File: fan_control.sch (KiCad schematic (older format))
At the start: 15 parts, among them M1 Fan, Q14 BC547, Q15 BC547, Q16 BC547, Q17 BC547, Q18 BC547

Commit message: footprint assoziation; pcb layout; and more
* delete mainboard pcb
* rearrange project files/names
* create pcb layout
* improve schematics
* more
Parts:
- removed Q14, Q15, Q16, Q17, Q18: BC547, Package_TO_SOT_THT:TO-92_Inline, symbol 0_project:BC547B
- removed R11, R15, R17, R19, R21: 10K, Resistor_THT:R_Axial_DIN0207_L6.3mm_D2.5mm_P15.24mm_Horizontal, symbol Device:R
- removed R14, R16, R18, R20: 22, Resistor_THT:R_Axial_DIN0207_L6.3mm_D2.5mm_P15.24mm_Horizontal, symbol Device:R
- added C2: elko, Capacitor_THT:CP_Radial_D5.0mm_P2.50mm, symbol 0_project:elko
- added D4: 1N4007, symbol Diode:1N4007
- added D6, D7, D8: 1N4007, Diode_THT:D_DO-41_SOD81_P2.54mm_Vertical_AnodeUp, symbol Diode:1N4007
- added Q2: IRFZ34N, Package_TO_SOT_THT:TO-220-3_Vertical, symbol 0_project:IRFZ34N
- added R2, R3: R, Resistor_THT:R_Axial_DIN0207_L6.3mm_D2.5mm_P2.54mm_Vertical, symbol Device:R
- added R4: 50k, Resistor_THT:R_Axial_DIN0207_L6.3mm_D2.5mm_P2.54mm_Vertical, symbol Device:R
- added U1: LM317_3PinPackage, Package_TO_SOT_THT:TO-220-3_Vertical, symbol Regulator_Linear:LM317_3PinPackage
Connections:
- net +15V: now also M1.1 (+), R2.2, U1.2 (VO)
- net multiplier/F+: now also Q2.2 (G), R4.1
- net GND: no longer names the net of M1.2 (-)
- net GND: now also Q2.1 (D)
- new net: C2.1, D7.1 (K), D8.1 (K), U1.3 (VI)
- new net: R2.1, R3.1, U1.1 (ADJ)
- new net +15VAC: D4.1 (K), D7.2 (A)
- new net 0: C2.2, D4.2 (A), D6.2 (A), Q2.3 (S), R3.2, R4.2
- new net 0VAC: D6.1 (K), D8.2 (A)
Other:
- note added: "Fan Transistor"
- moved on the sheet: M1

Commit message: progress on schematics
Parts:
- removed M1: Fan, Connector_PinHeader_2.54mm:PinHeader_1x02_P2.54mm_Vertical, symbol Motor:Fan
- removed Q2: IRFZ34N, Package_TO_SOT_THT:TO-220-3_Vertical, symbol 0_project:IRFZ34N
- removed R4: 50k, Resistor_THT:R_Axial_DIN0207_L6.3mm_D2.5mm_P2.54mm_Vertical, symbol Device:R
- added J1, J2, J3, J4, J5, J6, J7, J8: Conn_01x02_Male, Connector_PinHeader_2.54mm:PinHeader_1x02_P2.54mm_Vertical, symbol Connector:Conn_01x02_Male
- D4: footprint (none) -> Diode_THT:D_DO-41_SOD81_P2.54mm_Vertical_AnodeUp
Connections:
- net +15V: now also J4.1 (Pin_1), J4.2 (Pin_2)
- net +15VAC: now also J6.1 (Pin_1), J6.2 (Pin_2)
- net 0: now also J5.1 (Pin_1), J5.2 (Pin_2)
- net 0VAC: now also J8.1 (Pin_1), J8.2 (Pin_2)
- net B: now also J2.1 (Pin_1), J2.2 (Pin_2)
- net C: now also J3.1 (Pin_1), J3.2 (Pin_2)
- net E: now also J1.1 (Pin_1), J1.2 (Pin_2)
- new net F+: J7.1 (Pin_1), J7.2 (Pin_2)
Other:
- note removed: "Fan Transistor"
- moved on the sheet: R2, R3, U1

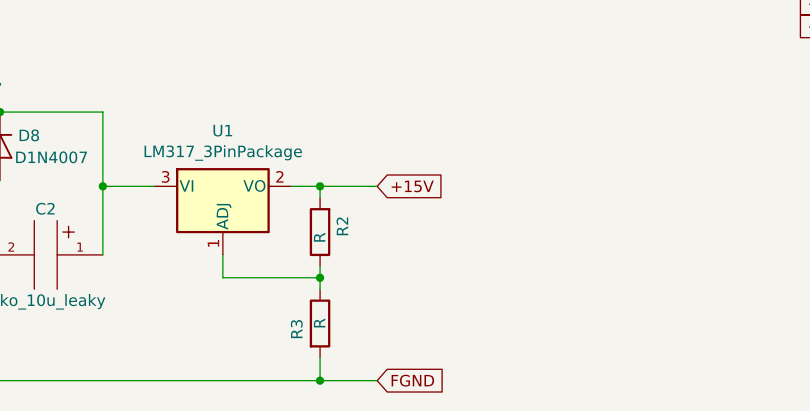
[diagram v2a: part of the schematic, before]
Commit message: add adjustment resistors
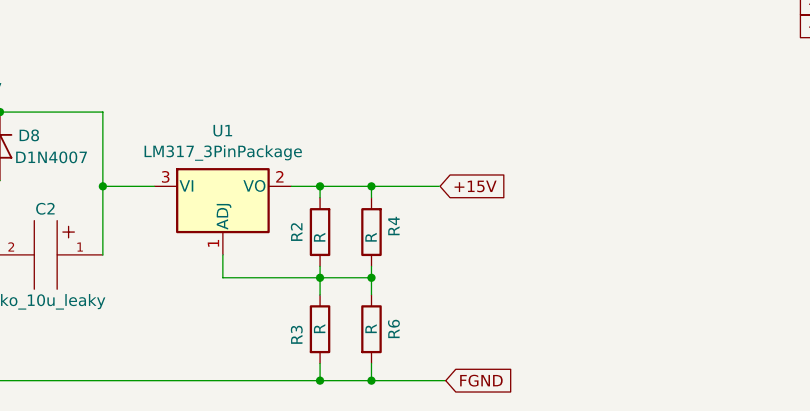
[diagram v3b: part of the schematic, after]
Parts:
- added R4, R6: R, Resistor_THT:R_Axial_DIN0207_L6.3mm_D2.5mm_P2.54mm_Vertical, symbol Device:R
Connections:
- net +15V: now also R4.2
- net 0: now also R6.2
- net at R2.1, R3.1, U1.1 (ADJ): now also R4.1, R6.1
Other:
- moved on the sheet: R3
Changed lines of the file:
@@
 L Device:R R3
 U 1 1 5EB4ABA5
-P 3250 4625
-F 0 "R3" V 3150 4600 50  0000 C CNN
-F 1 "R" V 3250 4625 50  0000 C CNN
-F 2 "Resistor_THT:R_Axial_DIN0207_L6.3mm_D2.5mm_P2.54mm_Vertical" V 3180 4625 50  0001 C CNN
-F 3 "~" H 3250 4625 50  0001 C CNN
-F 4 "N" H 3250 4625 50  0001 C CNN "Spice_Netlist_Enabled"
-	1    3250 4625
+P 3250 4650
+F 0 "R3" V 3150 4625 50  0000 C CNN
+F 1 "R" V 3250 4650 50  0000 C CNN
+F 2 "Resistor_THT:R_Axial_DIN0207_L6.3mm_D2.5mm_P2.54mm_Vertical" V 3180 4650 50  0001 C CNN
+F 3 "~" H 3250 4650 50  0001 C CNN
+F 4 "N" H 3250 4650 50  0001 C CNN "Spice_Netlist_Enabled"
+	1    3250 4650
 	1    0    0    -1
 $EndComp
@@
 	2825 4425 2825 4325
 Wire Wire Line
-	3250 4775 3250 4875
+	3250 4800 3250 4875
 Connection ~ 3250 4425
 Wire Wire Line
-	3250 4425 3250 4475
+	3250 4425 3250 4500
 Wire Wire Line
 	3250 4025 3250 4075
@@
 U 1 1 5EB4ABB4
 P 3250 4225
-F 0 "R2" V 3150 4200 50  0000 C CNN
+F 0 "R2" V 3350 4225 50  0000 C CNN
 F 1 "R" V 3250 4250 50  0000 C CNN
 F 2 "Resistor_THT:R_Axial_DIN0207_L6.3mm_D2.5mm_P2.54mm_Vertical" V 3180 4225 50  0001 C CNN
@@
 Connection ~ 3250 4025
 Wire Wire Line
-	3250 4875 3500 4875
-Wire Wire Line
-	3250 4025 3500 4025
+	3250 4875 3475 4875
+Wire Wire Line
+	3250 4025 3475 4025
 Wire Wire Line
 	1400 4875 3250 4875
 Connection ~ 3250 4875
-Text GLabel 3500 4025 2    50   Input ~ 0
+Text GLabel 3775 4025 2    50   Input ~ 0
 +15V
-Text GLabel 3500 4875 2    50   Input ~ 0
+Text GLabel 3800 4875 2    50   Input ~ 0
 FGND
 Text HLabel 1350 3700 1    50   Input ~ 0
@@
 Text GLabel 1800 1525 2    50   Input ~ 0
 F+
+Wire Wire Line
+	3250 4425 3475 4425
+$Comp
+L Device:R R4
+U 1 1 5EC4696D
+P 3475 4225
+F 0 "R4" V 3375 4200 50  0000 C CNN
+F 1 "R" V 3475 4250 50  0000 C CNN
+F 2 "Resistor_THT:R_Axial_DIN0207_L6.3mm_D2.5mm_P2.54mm_Vertical" V 3405 4225 50  0001 C CNN
+F 3 "~" H 3475 4225 50  0001 C CNN
+F 4 "N" H 3475 4225 50  0001 C CNN "Spice_Netlist_Enabled"
+	1    3475 4225
+	-1   0    0    1
+$EndComp
+$Comp
+L Device:R R6
+U 1 1 5EC46A56
+P 3475 4650
+F 0 "R6" V 3575 4650 50  0000 C CNN
+F 1 "R" V 3475 4650 50  0000 C CNN
+F 2 "Resistor_THT:R_Axial_DIN0207_L6.3mm_D2.5mm_P2.54mm_Vertical" V 3405 4650 50  0001 C CNN
+F 3 "~" H 3475 4650 50  0001 C CNN
+F 4 "N" H 3475 4650 50  0001 C CNN "Spice_Netlist_Enabled"
+	1    3475 4650
+	1    0    0    -1
+$EndComp
+Wire Wire Line
+	3475 4500 3475 4425
+Connection ~ 3475 4425
+Wire Wire Line
+	3475 4425 3475 4375
+Wire Wire Line
+	3475 4075 3475 4025
+Connection ~ 3475 4025
+Wire Wire Line
+	3475 4025 3775 4025
+Wire Wire Line
+	3475 4800 3475 4875
+Connection ~ 3475 4875
+Wire Wire Line
+	3475 4875 3800 4875
 $EndSCHEMATC

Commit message: add lm317 Vout calc text
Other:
- note added: "R3_6=1/(1/R3+1/R6)\nR2_4=1/(1/R2+1/R4)\nf=R3_6/R2_4\nV_Out = 1.25V ( 1+f)\n + I_adj*R3_6)"
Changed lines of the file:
@@
 Wire Wire Line
 	3475 4875 3800 4875
+Text Notes 2450 3600 0    50   ~ 0
+R3_6=1/(1/R3+1/R6)\nR2_4=1/(1/R2+1/R4)\nf=R3_6/R2_4\nV_Out = 1.25V ( 1+f)\n             + I_adj*R3_6)
 $EndSCHEMATC

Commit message: add resistors
...
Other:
- note added: "R3_6=1/(1/R3+1/R6)\nR2_4=1/(1/R2+1/R4)\nf=R3_6/R2_4\nV_Out = 1.25V ( 1+f)\n + I_adj*R3_6)\nI_adj aprox 0"
- note removed: "R3_6=1/(1/R3+1/R6)\nR2_4=1/(1/R2+1/R4)\nf=R3_6/R2_4\nV_Out = 1.25V ( 1+f)\n + I_adj*R3_6)"
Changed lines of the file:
@@
 	3475 4875 3800 4875
 Text Notes 2450 3600 0    50   ~ 0
-R3_6=1/(1/R3+1/R6)\nR2_4=1/(1/R2+1/R4)\nf=R3_6/R2_4\nV_Out = 1.25V ( 1+f)\n             + I_adj*R3_6)
+R3_6=1/(1/R3+1/R6)\nR2_4=1/(1/R2+1/R4)\nf=R3_6/R2_4\nV_Out = 1.25V ( 1+f)\n             + I_adj*R3_6)\nI_adj aprox 0
 $EndSCHEMATC
